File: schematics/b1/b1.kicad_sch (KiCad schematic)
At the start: 35 parts, among them SW6 SW_SPDT, U1 L7805, U8 AMS1117-3.3

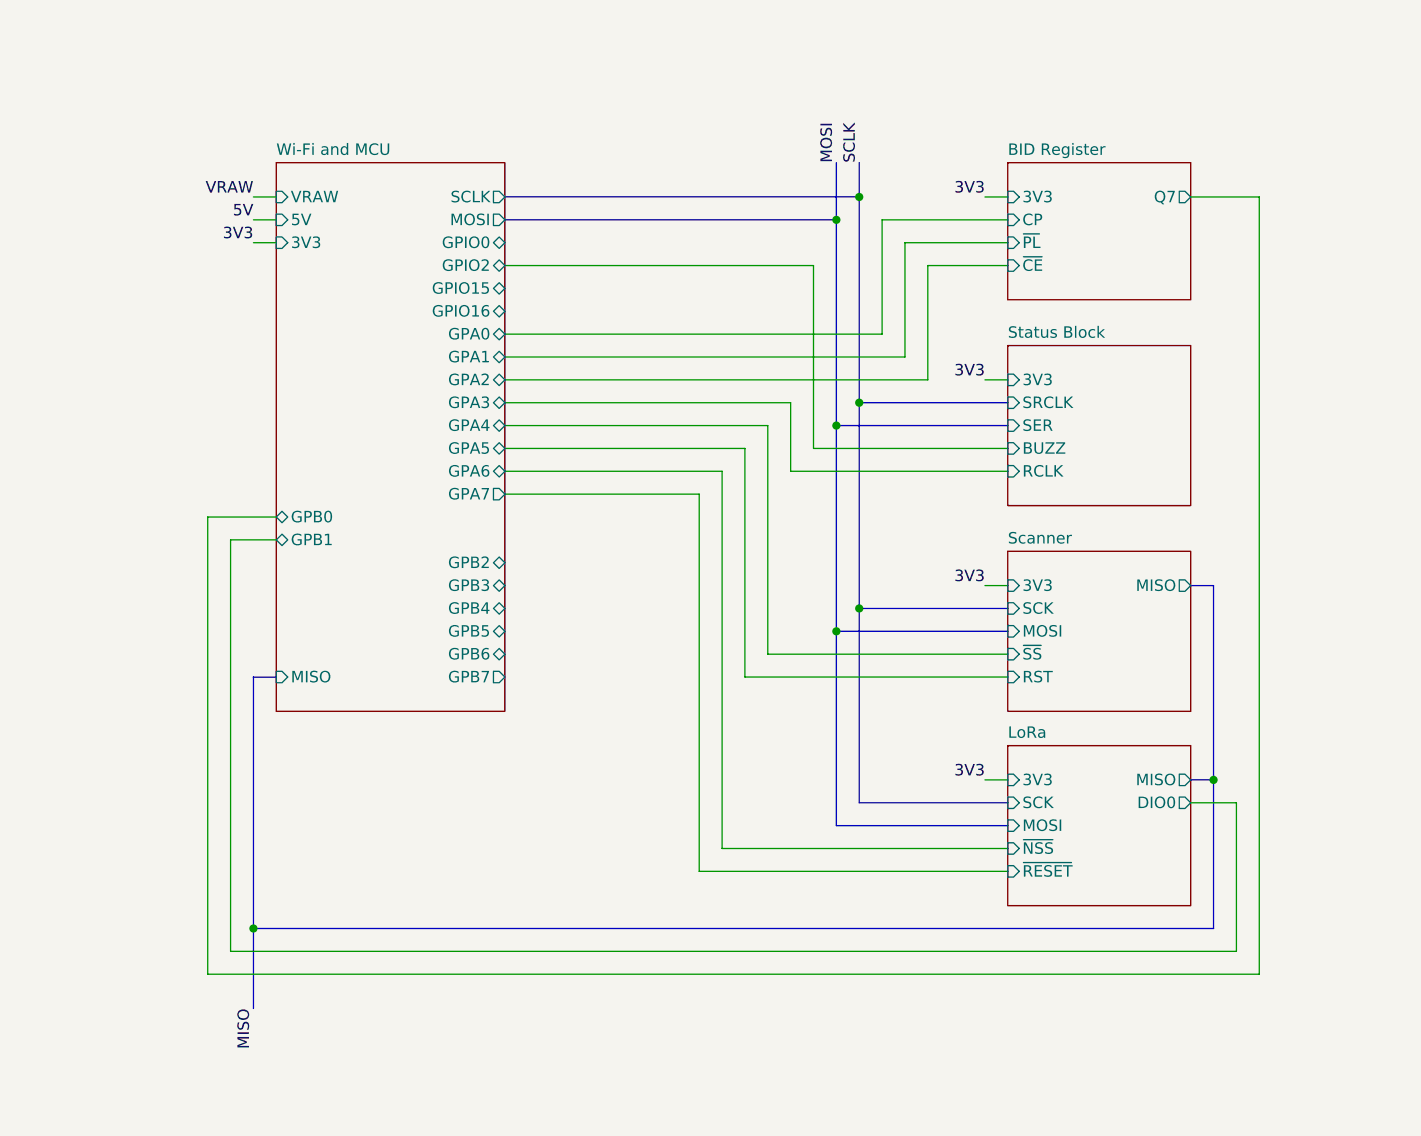
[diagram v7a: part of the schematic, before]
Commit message: Added optional interrupt pin to MCU for LoRa module.
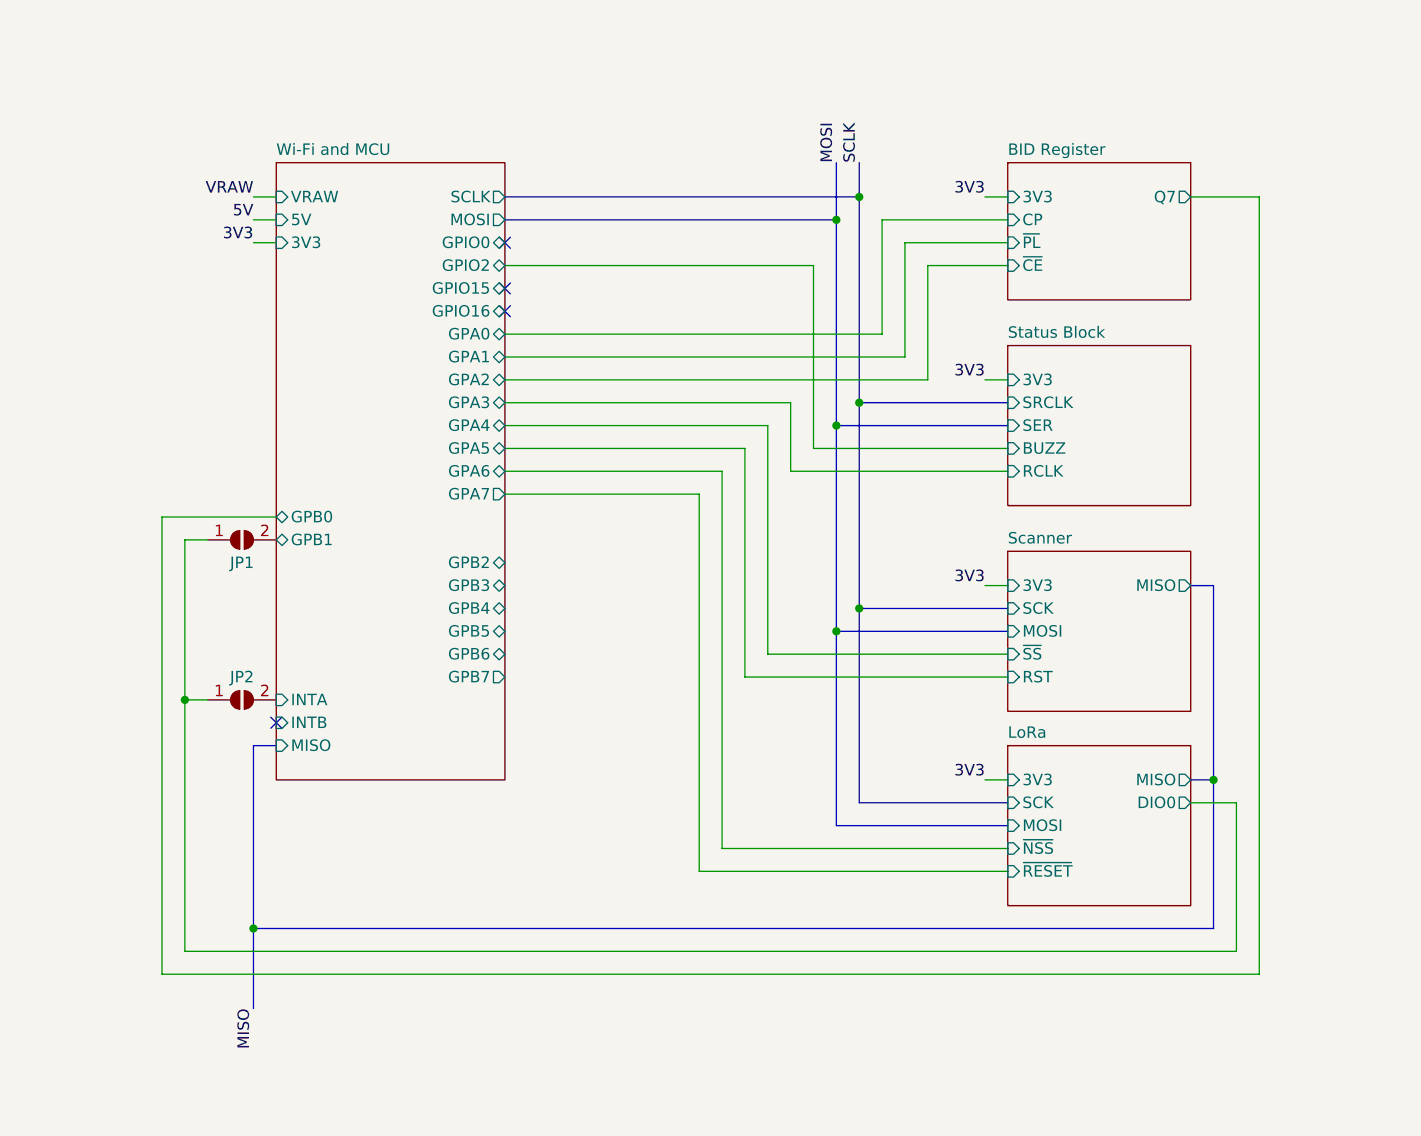
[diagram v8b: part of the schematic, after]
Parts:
- added JP1, JP2: SolderJumper_2_Open, symbol Jumper:SolderJumper_2_Open
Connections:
- net LoRa/DIO0: now also JP1.1 (A), JP2.1 (A)
- new net Wi-Fi and MCU/GPB1: JP1.2 (B)
- new net Wi-Fi and MCU/INTA: JP2.2 (B)
- no-connect marks 1 -> 5
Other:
- sheet Wi-Fi and MCU ports: added INTA, INTB; removed none
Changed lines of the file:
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@@
   (junction (at 34.29 143.51) (diameter 0) (color 0 0 0 0)
   )
+  (junction (at 142.24 99.06) (diameter 0) (color 0 0 0 0)
+  )
   (junction (at 99.06 39.37) (diameter 0) (color 0 0 0 0)
   )
@@
   (junction (at 217.17 66.04) (diameter 0) (color 0 0 0 0)
   )
+  (no_connect (at 177.8 48.26))
+  (no_connect (at 177.8 55.88))
+  (no_connect (at 177.8 53.34))
   (no_connect (at 22.86 34.29))
+  (no_connect (at 152.4 101.6))
   (wire (pts (xy 39.37 49.53) (xy 39.37 52.07))
     (stroke (width 0) (type default))
@@
     (stroke (width 0) (type default))
   )
-  (wire (pts (xy 147.32 81.28) (xy 152.4 81.28))
+  (wire (pts (xy 142.24 81.28) (xy 144.78 81.28))
     (stroke (width 0) (type default))
   )
@@
     (stroke (width 0) (type default))
   )
-  (wire (pts (xy 147.32 127) (xy 147.32 81.28))
+  (wire (pts (xy 142.24 127) (xy 142.24 99.06))
     (stroke (width 0) (type default))
   )
@@
     (stroke (width 0) (type default))
   )
-  (wire (pts (xy 144.78 78.74) (xy 152.4 78.74))
+  (wire (pts (xy 139.7 78.74) (xy 152.4 78.74))
     (stroke (width 0) (type default))
   )
@@
     (stroke (width 0) (type default))
   )
-  (wire (pts (xy 259.08 127) (xy 147.32 127))
+  (wire (pts (xy 259.08 127) (xy 142.24 127))
     (stroke (width 0) (type default))
   )
@@
     (stroke (width 0) (type default))
   )
-  (wire (pts (xy 144.78 129.54) (xy 144.78 78.74))
+  (wire (pts (xy 139.7 129.54) (xy 139.7 78.74))
     (stroke (width 0) (type default))
   )
@@
     (stroke (width 0) (type default))
   )
+  (wire (pts (xy 142.24 99.06) (xy 144.78 99.06))
+    (stroke (width 0) (type default))
+  )
   (wire (pts (xy 99.06 101.6) (xy 99.06 100.33))
     (stroke (width 0) (type default))
@@
     (stroke (width 0) (type default))
   )
-  (bus (pts (xy 149.86 96.52) (xy 152.4 96.52))
+  (bus (pts (xy 149.86 104.14) (xy 152.4 104.14))
     (stroke (width 0) (type default))
   )
@@
     (stroke (width 0) (type default))
   )
-  (wire (pts (xy 261.62 129.54) (xy 144.78 129.54))
+  (wire (pts (xy 261.62 129.54) (xy 139.7 129.54))
     (stroke (width 0) (type default))
   )
@@
     (stroke (width 0) (type default))
   )
+  (wire (pts (xy 142.24 99.06) (xy 142.24 81.28))
+    (stroke (width 0) (type default))
+  )
   (bus (pts (xy 256.54 86.36) (xy 256.54 107.95))
     (stroke (width 0) (type default))
@@
     (stroke (width 0) (type default))
   )
-  (bus (pts (xy 149.86 124.46) (xy 149.86 96.52))
+  (bus (pts (xy 149.86 124.46) (xy 149.86 104.14))
     (stroke (width 0) (type default))
   )
@@
     )
   )
+  (symbol (lib_id "Jumper:SolderJumper_2_Open") (at 148.59 99.06 0) (unit 1)
+    (in_bom yes) (on_board yes) (dnp no)
+    (property "Reference" "JP2" (at 148.59 96.52 0)
+      (effects (font (size 1.27 1.27)))
+    )
+    (property "Value" "SolderJumper_2_Open" (at 148.59 95.25 0)
+      (effects (font (size 1.27 1.27)) hide)
+    )
+    (property "Footprint" "" (at 148.59 99.06 0)
+      (effects (font (size 1.27 1.27)) hide)
+    )
+    (property "Datasheet" "~" (at 148.59 99.06 0)
+      (effects (font (size 1.27 1.27)) hide)
+    )
+    (pin "1")
+    (pin "2")
+    (instances
+      (project "b1"
+        (path "/d6142fa5-2354-4512-9919-37616259c364"
+          (reference "JP2") (unit 1)
+        )
+      )
+    )
+  )
   (symbol (lib_id "Switch:SW_SPDT") (at 25.4 29.21 270) (unit 1)
     (in_bom yes) (on_board yes) (dnp no) (fields_autoplaced)
@@
         (path "/d6142fa5-2354-4512-9919-37616259c364"
           (reference "TP29") (unit 1)
+        )
+      )
+    )
+  )
+  (symbol (lib_id "Jumper:SolderJumper_2_Open") (at 148.59 81.28 0) (unit 1)
+    (in_bom yes) (on_board yes) (dnp no)
+    (property "Reference" "JP1" (at 148.59 83.82 0)
+      (effects (font (size 1.27 1.27)))
+    )
+    (property "Value" "SolderJumper_2_Open" (at 148.59 77.47 0)
+      (effects (font (size 1.27 1.27)) hide)
+    )
+    (property "Footprint" "" (at 148.59 81.28 0)
+      (effects (font (size 1.27 1.27)) hide)
+    )
+    (property "Datasheet" "~" (at 148.59 81.28 0)
+      (effects (font (size 1.27 1.27)) hide)
+    )
+    (pin "1")
+    (pin "2")
+    (instances
+      (project "b1"
+        (path "/d6142fa5-2354-4512-9919-37616259c364"
+          (reference "JP1") (unit 1)
         )
       )
@@
     )
   )
-  (sheet (at 152.4 39.37) (size 25.4 60.96) (fields_autoplaced)
+  (sheet (at 152.4 39.37) (size 25.4 68.58) (fields_autoplaced)
     (stroke (width 0.1524) (type solid))
     (fill (color 0 0 0 0.0000))
@@
       (effects (font (size 1.27 1.27)) (justify left bottom))
     )
-    (property "Sheetfile" "wifi.kicad_sch" (at 152.4 100.9146 0)
+    (property "Sheetfile" "wifi.kicad_sch" (at 152.4 108.5346 0)
       (effects (font (size 1.27 1.27)) (justify left top) hide)
     )
@@
       (effects (font (size 1.27 1.27)) (justify right))
     )
-    (pin "MISO" input (at 152.4 96.52 180)
+    (pin "MISO" input (at 152.4 104.14 180)
       (effects (font (size 1.27 1.27)) (justify left))
     )
@@
       (effects (font (size 1.27 1.27)) (justify left))
     )
+    (pin "INTA" input (at 152.4 99.06 180)
+      (effects (font (size 1.27 1.27)) (justify left))
+    )
+    (pin "INTB" input (at 152.4 101.6 180)
+      (effects (font (size 1.27 1.27)) (justify left))
+    )
